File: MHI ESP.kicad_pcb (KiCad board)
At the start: 2 copper layers, 26 x 44 mm, 14 parts, among them J1 , Q1 BSS138, Q2 BSS138, Q3 BSS138, U1 WeMos_D1_mini, U2 LD1117S50TR

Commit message: Minor silkscreen updates and Gerber / Drill File Generation
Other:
- board text added: "1"
- board text added: "AC-WiFi v2.0"
- board text removed: "A/C-WiFi v2.0"
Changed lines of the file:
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@@
-(kicad_pcb (version 20171130) (host pcbnew "(5.1.2)-2")
+(kicad_pcb (version 20171130) (host pcbnew "(5.1.5)-3")
   (general
     (thickness 1.6)
-    (drawings 24)
+    (drawings 25)
     (tracks 78)
     (zones 0)
@@
       (outputformat 1)
       (mirror false)
-      (drillshape 1)
+      (drillshape 0)
       (scaleselection 1)
-      (outputdirectory ""))
+      (outputdirectory "Gerbers"))
   )
   (net 0 "")
@@
     (descr "16-pin module, column spacing 22.86 mm (900 mils), https://wiki.wemos.cc/products:d1:d1_mini, https://c1.staticflickr.com/1/734/31400410271_f278b087db_z.jpg")
     (tags "ESP8266 WiFi microcontroller")
-    (fp_text reference U1 (at 22 27) (layer F.SilkS)
+    (fp_text reference U1 (at 22 27) (layer F.SilkS) hide
       (effects (font (size 1 1) (thickness 0.15)))
     )
@@
     (tags "CMS SOT")
     (attr smd)
-    (fp_text reference U2 (at 0 -4.5) (layer F.SilkS)
+    (fp_text reference U2 (at 3.25 -3) (layer F.SilkS)
       (effects (font (size 1 1) (thickness 0.15)))
     )
@@
       (rotate (xyz 0 0 0))
     )
+  )
+  (gr_text 1 (at 117.5 80.25) (layer F.SilkS)
+    (effects (font (size 1.5 1.5) (thickness 0.3)))
   )
   (gr_line (start 130 76.5) (end 130 80) (layer F.Mask) (width 1.7))
@@
   (gr_line (start 115 77) (end 115 82) (layer Edge.Cuts) (width 0.05))
   (gr_line (start 117 75) (end 133 75) (layer Edge.Cuts) (width 0.05))
-  (gr_text "A/C-WiFi\nv2.0" (at 125 114 180) (layer B.SilkS)
+  (gr_text "AC-WiFi\nv2.0" (at 125 114 180) (layer B.SilkS)
     (effects (font (size 2.5 2.5) (thickness 0.5)) (justify mirror))
   )
@@
   (gr_line (start 135 119) (end 115 119) (layer Edge.Cuts) (width 0.05))
   (gr_line (start 138 87) (end 138 116) (layer Edge.Cuts) (width 0.05))
-  (via (at 129 103) (size 0.6) (drill 0.3) (layers F.Cu B.Cu) (net 3))
-  (via (at 133 101.5) (size 0.6) (drill 0.3) (layers F.Cu B.Cu) (net 3))
-  (segment (start 124.9375 107.9375) (end 126.5 107.9375) (width 0.5) (layer F.Cu) (net 5))
-  (segment (start 124 107) (end 124.9375 107.9375) (width 0.5) (layer F.Cu) (net 5))
-  (segment (start 124.9375 102.9375) (end 126.5 102.9375) (width 0.5) (layer F.Cu) (net 3))
-  (segment (start 124 102) (end 124.9375 102.9375) (width 0.5) (layer F.Cu) (net 3))
   (segment (start 130 76.5) (end 130 80) (width 1.7) (layer F.Cu) (net 1))
   (via (at 130 76.5) (size 1.7) (drill 0.95) (layers F.Cu B.Cu) (net 1))
@@
   (segment (start 128.28 110.28) (end 136.36 110.28) (width 0.75) (layer B.Cu) (net 2))
   (segment (start 126.5 108.5) (end 128.28 110.28) (width 0.75) (layer B.Cu) (net 2))
+  (via (at 129 103) (size 0.6) (drill 0.3) (layers F.Cu B.Cu) (net 3))
+  (via (at 133 101.5) (size 0.6) (drill 0.3) (layers F.Cu B.Cu) (net 3))
+  (segment (start 124.9375 102.9375) (end 126.5 102.9375) (width 0.5) (layer F.Cu) (net 3))
+  (segment (start 124 102) (end 124.9375 102.9375) (width 0.5) (layer F.Cu) (net 3))
   (segment (start 127.5 76.5) (end 127.5 80) (width 1.7) (layer F.Cu) (net 3))
   (via (at 127.5 76.5) (size 1.7) (drill 0.95) (layers F.Cu B.Cu) (net 3))
@@
   (segment (start 129 88) (end 129 97.5) (width 0.5) (layer F.Cu) (net 4))
   (segment (start 129 97.5) (end 128.5625 97.9375) (width 0.5) (layer F.Cu) (net 4))
+  (segment (start 124.9375 107.9375) (end 126.5 107.9375) (width 0.5) (layer F.Cu) (net 5))
+  (segment (start 124 107) (end 124.9375 107.9375) (width 0.5) (layer F.Cu) (net 5))
   (segment (start 125 76.5) (end 125 80) (width 1.7) (layer F.Cu) (net 5))
   (via (at 125 76.5) (size 1.7) (drill 0.95) (layers F.Cu B.Cu) (net 5))

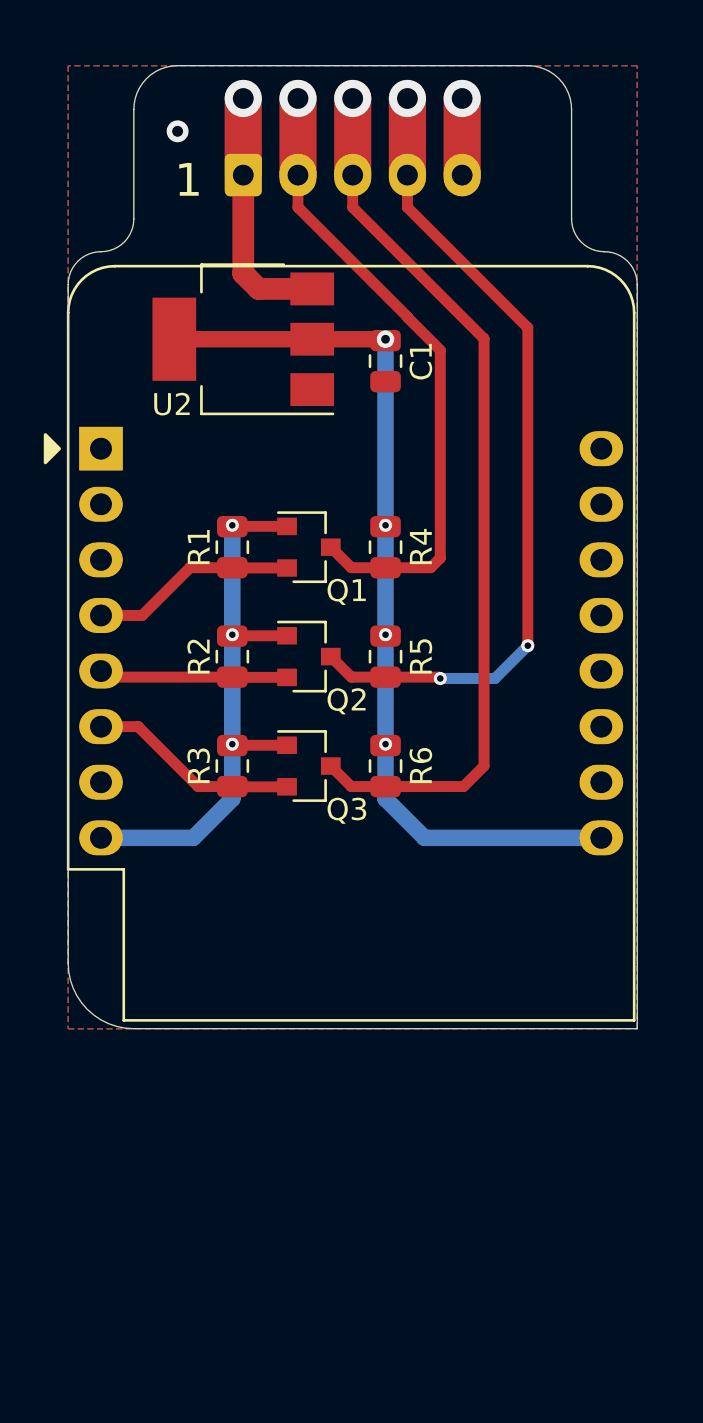
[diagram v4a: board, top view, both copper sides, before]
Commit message: Added IR data injection circuit and headers
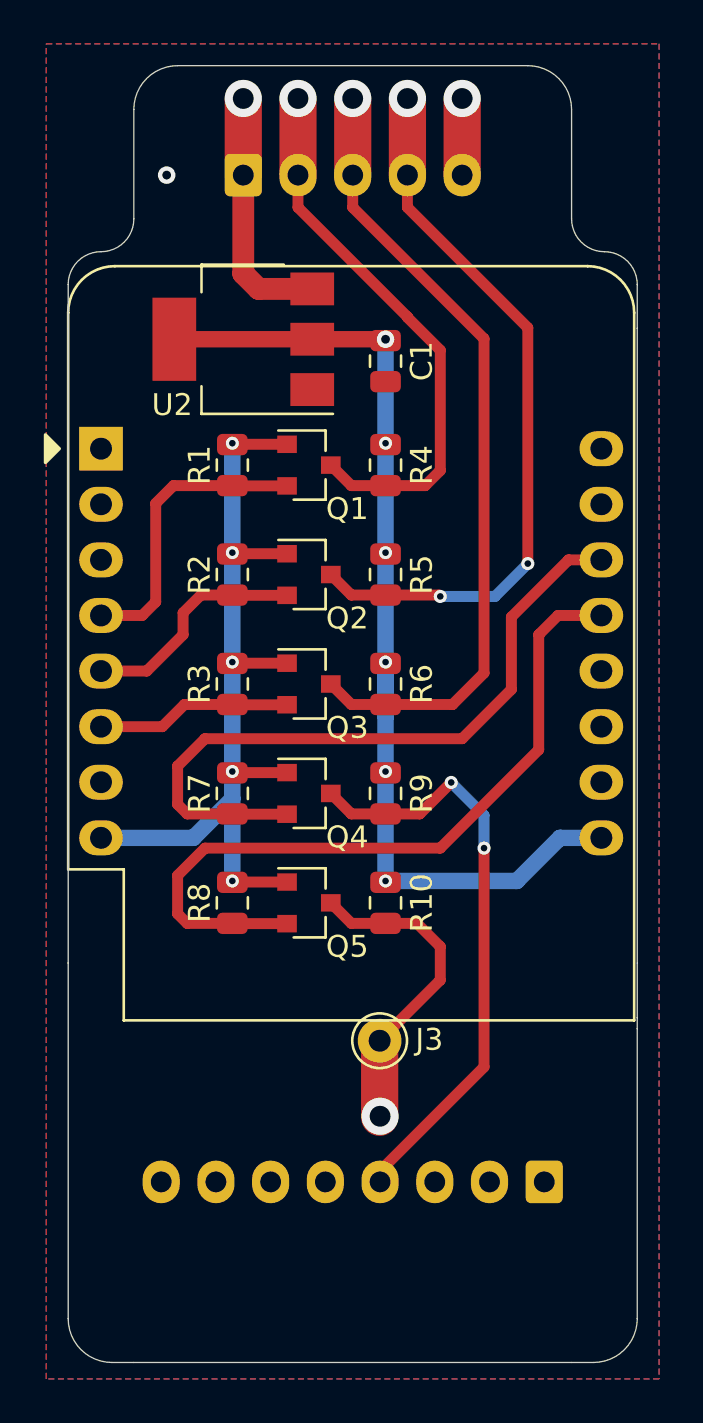
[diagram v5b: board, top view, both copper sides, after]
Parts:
- added J2: DISPLAY, Connector_JST:JST_XH_S8B-XH-A-1_1x08_P2.50mm_Horizontal, B.Cu at (133.8, 126.0)
- added J3: Conn_01x01_Male, Connector_Pin:Pin_D1.0mm_L10.0mm, F.Cu at (126.2, 119.5)
- added Q4: BSS138, Package_TO_SOT_SMD:SOT-23, F.Cu at (123.0, 108.2)
- added Q5: BSS138, Package_TO_SOT_SMD:SOT-23, F.Cu at (123.0, 113.2)
- added R10: 10k, Resistor_SMD:R_0805_2012Metric, F.Cu at (126.5, 113.2)
- added R7: 10k, Resistor_SMD:R_0805_2012Metric, F.Cu at (119.5, 108.2)
- added R8: 10k, Resistor_SMD:R_0805_2012Metric, F.Cu at (119.5, 113.2)
- added R9: 10k, Resistor_SMD:R_0805_2012Metric, F.Cu at (126.5, 108.2)
- J1: value (none) -> CNS
- moved Q1 3.75 mm to (123.0, 93.2)
- moved Q2 3.75 mm to (123.0, 98.2)
- moved Q3 3.75 mm to (123.0, 103.2)
- moved R1 3.75 mm to (119.5, 93.2)
- moved R2 3.75 mm to (119.5, 98.2)
- moved R3 3.75 mm to (119.5, 103.2)
- moved R4 3.75 mm to (126.5, 93.2)
- moved R5 3.75 mm to (126.5, 98.2)
- moved R6 3.75 mm to (126.5, 103.2)
- moved REF** 0.75 mm to (125.0, 95.2)
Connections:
- U1 pad 13: (no net) -> ESP-IRDOUT
- U1 pad 14: (no net) -> ESP-IRDIN
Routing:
- net ESP-IRDOUT: track 0.00 -> 34.3 mm
- net ESP-IRDIN: track 0.00 -> 32.1 mm
- net IRDIN: track 0.00 -> 27.3 mm, vias 0 -> 2
- net IRDOUT: track 0.00 -> 14.8 mm, vias 0 -> 1
- net +3V3: track 26.8 -> 39.2 mm, vias 3 -> 5
- net +5V: track 41.2 -> 47.6 mm, vias 4 -> 6
- net ESP-SCK: track 9.41 -> 13.6 mm
- net MHI-MOSI: track 40.8 -> 36.7 mm
- net MHI-SCK: track 29.3 -> 25.4 mm
- net MHI-MISO: track 37.3 -> 33.6 mm
- net ESP-MISO: track 8.62 -> 10.9 mm
- net ESP-MOSI: track 9.64 -> 8.92 mm
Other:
- board size 26 x 44 mm -> 26 x 59.2 mm
- board text added: "AC-WiFi v3.0"
- board text removed: "1"
- board text removed: "AC-WiFi v2.0"
